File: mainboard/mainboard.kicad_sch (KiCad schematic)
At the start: 0 parts

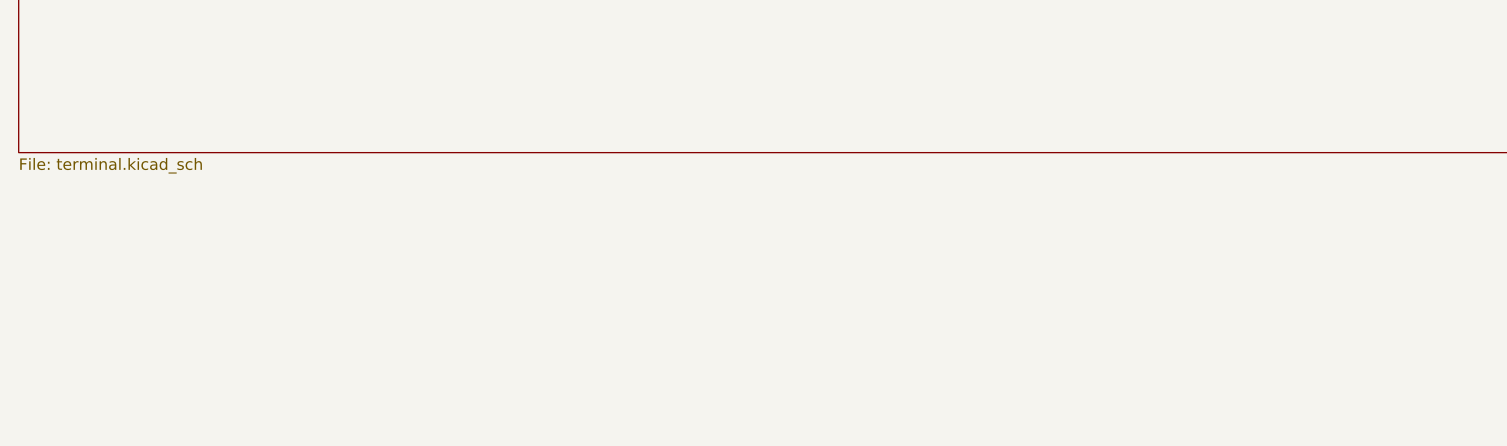
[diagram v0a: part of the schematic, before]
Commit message: merged /transformers with /mainboard
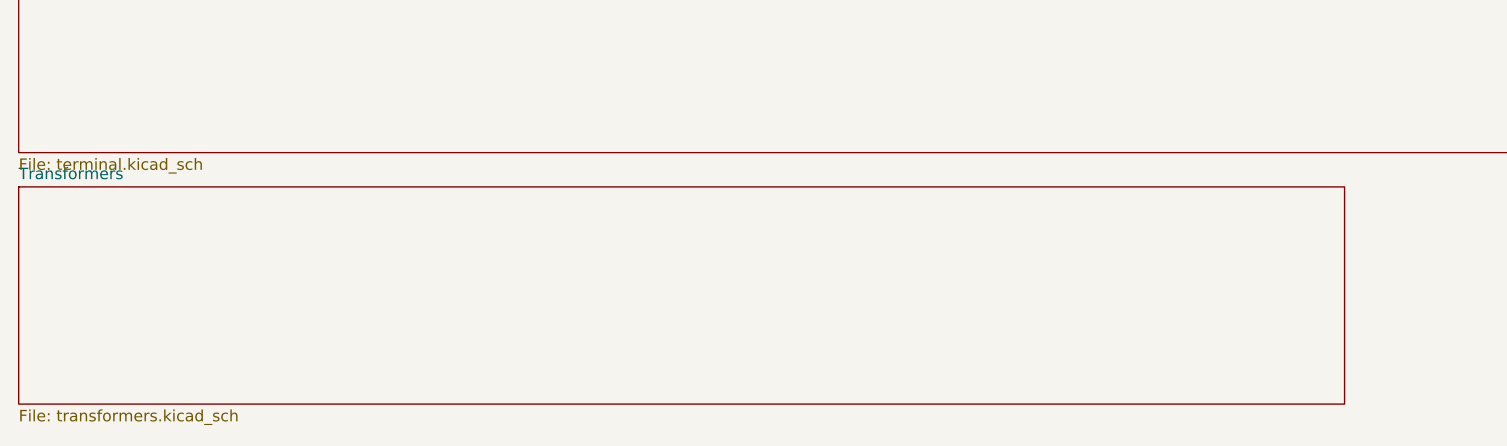
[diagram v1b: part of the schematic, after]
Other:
- added sheet Transformers (transformers.kicad_sch)
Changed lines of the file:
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@@
+		)
+	)
+	(sheet
+		(at 22.86 168.91)
+		(size 147.32 24.13)
+		(exclude_from_sim no)
+		(in_bom yes)
+		(on_board yes)
+		(dnp yes)
+		(fields_autoplaced yes)
+		(stroke
+			(width 0.1524)
+			(type solid)
+		)
+		(fill
+			(color 0 0 0 0)
+		)
+		(property "Sheetname" "Transformers"
+			(at 22.86 168.1984 0)
+			(show_name no)
+			(do_not_autoplace no)
+			(effects
+				(font
+					(size 1.27 1.27)
+				)
+				(justify left bottom)
+			)
+		)
+		(property "Sheetfile" "transformers.kicad_sch"
+			(at 22.86 193.6246 0)
+			(show_name no)
+			(do_not_autoplace no)
+			(effects
+				(font
+					(size 1.27 1.27)
+				)
+				(justify left top)
+			)
+		)
+		(instances
+			(project "mainboard"
+				(path "/b38b6155-24ef-4e7a-9d9a-2cb213939c19"
+					(page "5")
+				)
+			)
 		)
 	)

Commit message: added kicad drawing template
new file:   boardfont.svg
new file:   img/00101P3.png
new file:   mainboard/apple1template.kicad_wks
additional work on mainboard
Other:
- title: Apple I -> Processor Section
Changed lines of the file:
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@@
 	(paper "A4")
 	(title_block
-		(title "Apple I")
+		(title "Processor Section")
 		(date "2019-08-11")
 		(comment 1 "Drawn by Nicolas Robin")

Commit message: board is now complete, cleanup work can begin
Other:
- title: Processor Section -> Apple I - Processor Section
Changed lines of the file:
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@@
 	(paper "A4")
 	(title_block
-		(title "Processor Section")
+		(title "Apple I - Processor Section")
 		(date "2019-08-11")
 		(comment 1 "Drawn by Nicolas Robin")
